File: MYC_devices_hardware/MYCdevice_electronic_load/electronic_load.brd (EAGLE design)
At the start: 116.8 x 55.5 mm, 118 parts, among them IC1 ATMEGA644A, IC10 MCP4921, IC11 LM324N, IC12 LM324N, IC13 79L09, IC14 MCP4921, IC2 MAX232, IC21 MCP60x4, IC22 MCP60x4, IC3 PCA9517, IC4 78L5, IC5 MCP4921, IC6 MCP4921, IC7 MCP4921, IC8 MCP4921, IC9 MCP4921, Q1 20MHz, T1 BC807, T2 BC817, X1 8-15V, X4 RS232

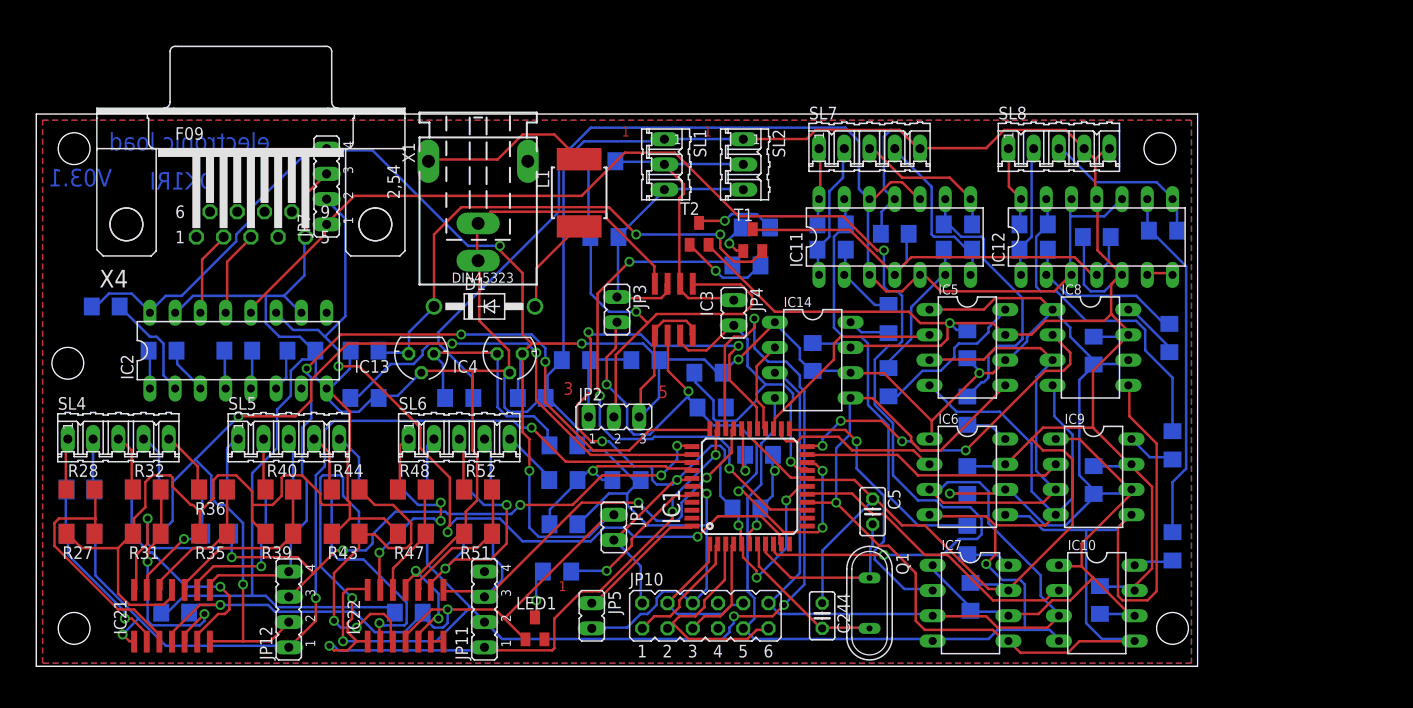
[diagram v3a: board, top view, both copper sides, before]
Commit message: board with 16bit AD + corresponding firmware + doc
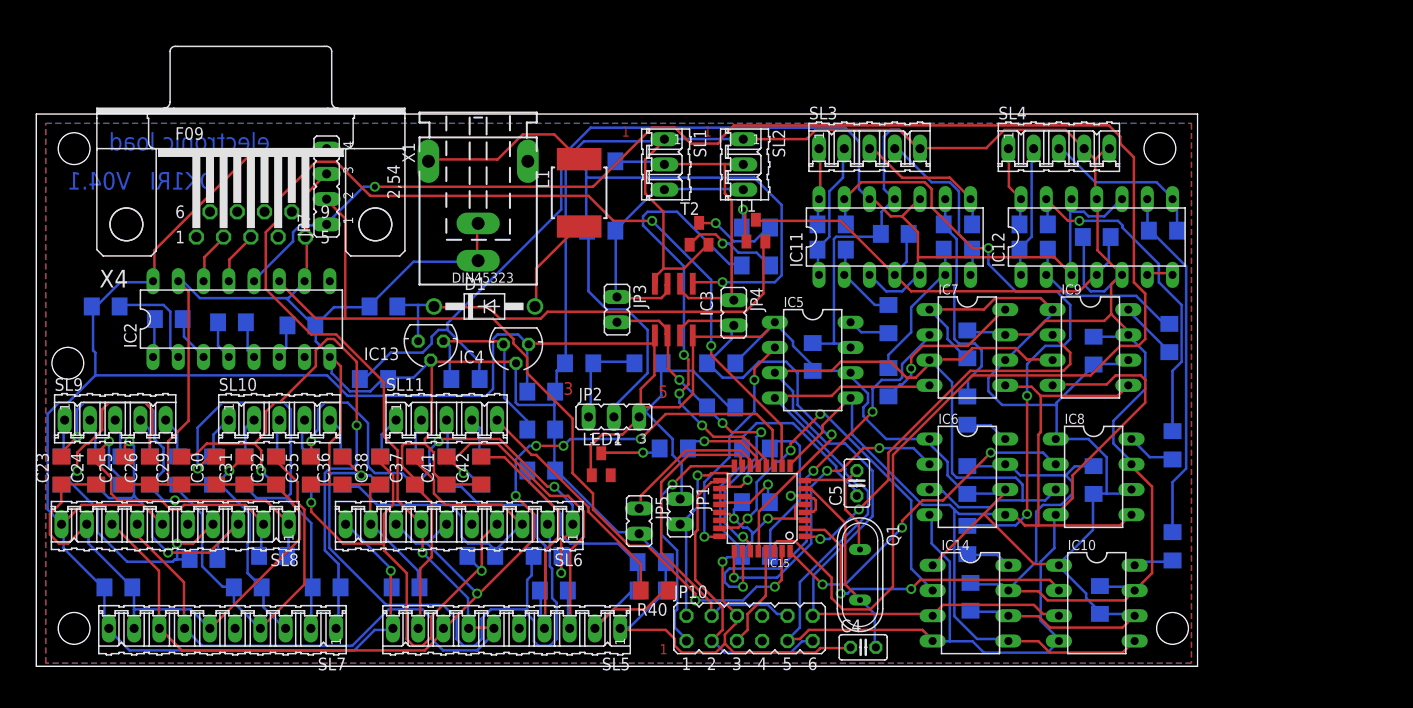
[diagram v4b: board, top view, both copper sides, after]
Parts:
- removed C244: 18pF, resistor:C025-025X050
- removed IC1: ATMEGA644A, atmel:TQFP44
- removed IC21, IC22: MCP60x4, linear:SO14
- removed JP11, JP12: (no value), jumper:JP4
- removed R41, R43, R45, R47, R49, R51: 154k, resistor:M1206
- removed R42, R44, R46, R48, R50, R52: 18k, resistor:M1206
- removed R53: 180, resistor:R1206
- removed R54: 1k5, resistor:R1206
- added C23, C24, C25, C26, C29, C30, C31, C32, C35, C36, C37, C38, C41, C42: 22n, resistor:C1206
- added C27, C28, C33, C34, C39, C40, C43: 220n, resistor:C1206
- added C50, C51: 22uF, rcl:C1206
- added IC15: MEGA8-AI, atmel:TQFP32-08
- added R12: 100, resistor:R1206
- added SL10, SL9: Iin, con-amp-quick:05P
- added SL11: U/Iin, con-amp-quick:05P
- added SL3: Gates1, con-amp-quick:05P
- C4: value 22uF -> 18pF; device rcl:C1206 -> resistor:C025-025X050
- JP10: value (none) -> ISP
- R25, R27, R29, R33, R35, R37: value 154k -> 100; device resistor:M1206 -> resistor:R1206
- R26, R30, R32, R34, R36: value 18k -> 100; device resistor:M1206 -> resistor:R1206
- R28: value 18k -> 100
- R31: value 154 -> 100; device resistor:M1206 -> resistor:R1206
- R38: value 18k -> see maunual; device resistor:M1206 -> resistor:R1206
- R39: value 154k -> see manual; device resistor:M1206 -> resistor:R1206
- R40: value 18k -> 2k2; device resistor:M1206 -> resistor:R1206
- SL4: value Iin -> Gates2
- SL5: value Iin -> AD_F1_U; device con-amp-quick:05P -> con-amp-quick:10P
- SL6: value U/Iin -> AD_F3_F2; device con-amp-quick:05P -> con-amp-quick:10P
- SL7: value Gates1 -> AD_F5_F4; device con-amp-quick:05P -> con-amp-quick:10P
- SL8: value Gates2 -> ADF7_F6; device con-amp-quick:05P -> con-amp-quick:10P
- moved SL4 99.0 mm to (102.9, 52.1)
- moved SL8 96.6 mm to (14.0, 14.3), turned to 180 degrees
- moved SL7 81.0 mm to (18.7, 3.81), turned to 180 degrees
- moved R40 39.1 mm to (62.2, 7.62), turned to 180 degrees
- moved R38 38.8 mm to (61.9, 7.62)
- moved R39 37.6 mm to (61.9, 10.5), flipped to the bottom
- moved IC14 29.1 mm to (94.0, 6.35)
- moved SL5 29.0 mm to (47.3, 3.81), turned to 180 degrees
- moved IC7 25.7 mm to (93.7, 32.1)
- moved R36 23.6 mm to (41.3, 19.7), flipped to the bottom, turned to 270 degrees
- moved R35 21.3 mm to (38.1, 19.7), flipped to the bottom, turned to 270 degrees
- moved R37 21.3 mm to (44.8, 19.7), turned to 270 degrees
- moved C4 18.3 mm to (83.2, 1.91), flipped to the top, turned to 0 degrees
- moved LED1 17.8 mm to (56.8, 20.3)
- moved R11 17.1 mm to (64.1, 21.9)
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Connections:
- removed net I1: IC1.36, IC21.1, JP12.1, R25.2
- removed net I2: IC1.35, IC21.7, JP12.2, R29.2
- removed net I3: IC1.34, IC21.14, JP12.3, R33.2
- removed net I4: IC1.33, IC21.8, JP12.4, R37.2
- removed net I5: IC1.32, IC22.1, JP11.1, R41.2
- removed net I6: IC1.31, IC22.14, JP11.2, R45.2
- removed net I7: IC1.30, IC22.8, JP11.3, R49.2
- removed net N$2: IC1.9, IC2.12, JP7.1
- removed net N$25: C3.2, IC1.29
- removed net N$34: IC22.13, R45.1, R46.1
- removed net N$41: IC21.13, R33.1, R34.1
- removed net N$44: IC21.10, R39.1, R40.2
- removed net N$47: IC22.2, R41.1, R42.1
- removed net N$52: R48.1, SL6.1
- removed net N$53: R46.2, SL6.2
- removed net N$65: R28.1, SL4.1
- removed net N$66: R32.1, SL4.3
- removed net N$67: IC21.3, R27.1, R28.2
- removed net N$68: R36.2, SL4.5
- removed net N$69: R26.2, SL4.2
- removed net N$79: R34.2, SL5.1
- removed net N$80: IC21.12, R35.1, R36.1
- removed net N$89: R50.2, SL6.4
- removed net N$90: IC22.10, R51.1, R52.2
- new net I1N: R37.1, SL11.4
- new net I1P: R36.1, SL11.3
- new net I2N: R35.1, SL11.2
- new net I2P: R34.1, SL11.1
- new net I3N: R33.1, SL10.5
- new net I3P: R32.1, SL10.4
- new net I4N: R31.1, SL10.3
- new net I4P: R30.1, SL10.2
- new net I5N: R29.1, SL10.1
- new net I5P: R28.1, SL9.5
- new net I6N: R27.1, SL9.4
- new net I6P: R26.1, SL9.3
- new net I7N: R25.1, SL9.2
- new net I7P: R12.1, SL9.1
- new net N$71: C25.2, C27.2, R25.2, SL8.3
- new net N$78: C41.2, C43.1, R37.2, SL5.3
- new net SCL2: IC15.11, SL5.8, SL6.6, SL6.8, SL7.8, SL8.8
- new net SDA2: IC15.10, SL5.6, SL5.7, SL6.7, SL7.7, SL8.7
- net FET1: now also IC10.2, IC15.2; no longer IC1.23, IC7.2
- net FET2: now also IC15.1, IC9.2; no longer IC1.26, IC14.2
- net FET3: now also IC15.32, IC8.2; no longer IC1.24, IC6.2
- net FET4: now also IC15.26, IC7.2; no longer IC1.25, IC5.2
- net FET5: now also IC15.25, IC6.2; no longer IC1.21, IC9.2
- net FET6: now also IC15.24, IC5.2; no longer IC1.22, IC8.2
- net FET7: now also IC14.2, IC15.23; no longer IC1.16, IC10.2
- net GND: now also C23.1, C24.1, C25.1, C26.1, C29.1, C30.1, C31.1, C32.1, C35.1, C36.1, C37.1, C38.1, C4.1, C41.1, C42.1, C50.2, C51.1, IC15.21, IC15.3, IC15.5, R38.2, SL3.5, SL4.4, SL4.5, SL5.1, SL5.9, SL6.9, SL7.6, SL7.9, SL8.9; no longer C244.1, C4.2, IC1.18, IC1.28, IC1.39, IC1.6, IC21.11, IC22.11, IC22.5, R27.2, R31.2, R35.2, R43.2, R47.2, R51.2, R54.2, SL7.5, SL8.4, SL8.5
- net GON: now also IC15.12; no longer IC1.14
- net LDAC: now also IC15.9; no longer IC1.15
- net N$1: now also C26.2, C27.1, R12.2, SL8.4; no longer IC21.2, R25.1, R26.1
- net N$11: now also IC15.8; no longer IC1.8
- net N$15: now also IC15.16; no longer IC1.2
- net N$18: now also IC15.29; no longer IC1.4
- net N$19: now also C4.2, IC15.7; no longer C244.2, IC1.7
- net N$21: now also IC14.8; no longer IC7.8
- net N$23: now also IC15.15; no longer IC1.1
- net N$24: now also IC9.8; no longer IC8.8
- net N$26: now also IC8.8; no longer IC9.8
- net N$27: now also R40.2, SL11.5; no longer R53.2, SL6.5
- net N$29: now also C31.2, C33.1, R29.2, SL7.3; no longer R30.2, SL4.4
- net N$30: now also C30.2, C34.2, R30.2, SL7.2; no longer IC21.6, R29.1, R30.1
- net N$31: now also IC5.8; no longer IC14.8
- net N$32: now also C29.2, C34.1, R31.2, SL7.1; no longer IC22.9, R49.1, R50.1
- net N$35: now also IC15.27; no longer IC1.20
- net N$37: now also IC15.14; no longer IC1.44
- net N$4: now also C50.1, C51.2, IC15.18, IC15.4, IC15.6; no longer C4.1, IC1.17, IC1.27, IC1.38, IC1.5
- net N$42: now also IC15.30, IC2.12, JP7.1; no longer IC1.40, R11.1
- net N$45: now also C38.2, C39.2, R32.2, SL6.4; no longer IC21.9, R37.1, R38.1
- net N$46: now also IC15.17; no longer IC1.3
- net N$48: now also C37.2, C39.1, R33.2, SL6.3; no longer R44.1, SL5.4
- net N$49: now also C36.2, C40.2, R34.2, SL6.2; no longer IC21.5, R31.1, R32.2
- net N$50: now also IC15.28; no longer IC1.19
- net N$54: now also IC15.13, R11.1; no longer R38.2, SL5.3
- net N$55: now also IC7.8; no longer IC5.8
- net N$6: now also IC15.31; no longer IC1.10
- net N$60: now also C3.2, IC15.20; no longer R42.2, SL5.5
- net N$70: now also C24.2, C28.1, R26.2, SL8.2; no longer R40.1, SL5.2
- net N$72: now also C35.2, C40.1, R35.2, SL6.1; no longer IC22.3, R43.1, R44.2
- net N$74: now also C23.2, C28.2, R27.2, SL8.1; no longer IC22.12, R47.1, R48.2
- net N$76: now also C42.2, C43.2, R36.2, SL5.4; no longer R52.1, SL6.3
- net N$8: now also C32.2, C33.2, R28.2, SL7.4; no longer IC22.6, IC22.7
- net SFET1: now also IC12.8, R24.2, SL4.3; no longer IC11.14, R18.2, SL7.1
- net SFET2: now also IC12.1, R20.2, SL4.2; no longer IC11.1, R14.2, SL7.2
- net SFET3: now also IC12.14, R22.2, SL4.1; no longer IC11.8, R16.2, SL7.3
- net SFET4: now also SL3.4; no longer SL7.4
- net SFET5: now also IC11.8, R16.2, SL3.3; no longer IC12.14, R22.2, SL8.1
- net SFET6: now also IC11.1, R14.2, SL3.2; no longer IC12.1, R20.2, SL8.2
- net SFET7: now also IC11.14, R18.2, SL3.1; no longer IC12.8, R24.2, SL8.3
- net U: now also R38.1, R39.1, R40.1, SL5.2; no longer IC1.37, R53.1, R54.1
- net VDD: now also SL5.10, SL6.10, SL7.10, SL8.10, SL8.6; no longer IC21.4, IC22.4
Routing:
- net SDA2: track 0.00 -> 177.8 mm, vias 0 -> 3
- net N$42: track 15.8 -> 178.8 mm
- net N$2: track 136.6 -> 0.00 mm, vias 2 -> 0
- net I6: track 111.8 -> 0.00 mm, vias 4 -> 0
- net SCL2: track 0.00 -> 110.9 mm, vias 0 -> 5
- net I2: track 101.8 -> 0.00 mm, vias 4 -> 0
- net I1: track 92.9 -> 0.00 mm, vias 3 -> 0
- net I5: track 84.7 -> 0.00 mm, vias 4 -> 0
- net I4: track 82.1 -> 0.00 mm, vias 3 -> 0
- net I3: track 78.7 -> 0.00 mm, vias 6 -> 0
- net N$4: track 99.7 -> 48.5 mm, vias 7 -> 3
- net I7: track 47.8 -> 0.00 mm, vias 2 -> 0
- net VDD: track 378.0 -> 423.7 mm, vias 8 -> 1
- net N$49: track 24.3 -> 67.4 mm, vias 2 -> 1
- net N$76: track 5.42 -> 44.9 mm
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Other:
- board text added: "V04.1"
- board text removed: "V03.1"
